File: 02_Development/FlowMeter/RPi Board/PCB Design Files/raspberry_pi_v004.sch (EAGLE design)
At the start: 116 parts, among them J5 POWER_JACK, P1 SPL006-007, P2 SPL006-007, P3 SPL006-007, P4 SPL006-007, P5 SPL006-007, Q1 4.3A/20V/54mΩ, Q2 500mA/300V, U6 TCA9548APWR, U7 TCA9548APWR

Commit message: added new 5V regulator
added new 5V regulator as existing regulator was out-of-stock at JLCPCB
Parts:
- removed C13: 33n, SparkFun-Capacitors:CAP-0805
- removed C23: 1uF, SparkFun-Capacitors:CAP-0805
- removed D3: 3A/40V/500mV, SparkFun-DiscreteSemi:DIODE-SCHOTTKY-B340A
- removed L1: INDUCTOR12.5, th_libraries:INDUCTOR12.5
- removed R1: 10K, SparkFun-Resistors:0.3OHM-0805-1/8W-1%
- removed R2: 3.3K, SparkFun-Resistors:0.3OHM-0805-1/8W-1%
- removed VREG1: XL4015, th_libraries:XL4015
- added C24: 100nF, SparkFun-Capacitors:CAP-0805
- added C25: 22uF, microbuilder:CAP_CERAMIC0805-NOOUTLINE
- added C27: 10uF, microbuilder:CAP_CERAMIC0805-NOOUTLINE
- added C28: 470nF, SparkFun-Capacitors:CAP-0805
- added C29: 4.7pF, SparkFun-Capacitors:CAP-0603
- added INDUCT: INDUCTOR_6.6_7.3, th_libraries:INDUCTOR_6.6_7.3
- added R49: 365K, SparkFun-Passives:RESISTOR0805-RES
- added R50: 49.9K, SparkFun-Passives:RESISTOR0805-RES
- added R51: 100K, SparkFun-Passives:RESISTOR0805-RES
- added R52: 10K, SparkFun-Resistors:0.3OHM-0805-1/8W-1%
- added TPS: TPS56528, th_libraries:TPS56528
- C19: value 1uF -> 10uF; device SparkFun-Capacitors:CAP-0805 -> microbuilder:CAP_CERAMIC0805-NOOUTLINE
- C20: value 1uF -> 100nF
- C22: value 220uF -> 22uF; device SparkFun-Capacitors:560UF-PANASONIC_G-25V-20% -> microbuilder:CAP_CERAMIC0805-NOOUTLINE
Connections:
- new net N$14: C24.1, TPS.VBST
- new net N$17: R51.1, TPS.PG
- new net N$27: R52.2, TPS.EN
- net 12V: now also C21.+, C27.1, R52.1, TPS.VIN; no longer C22.+, VREG1.IN
- net 5V: now also C22.1, C25.1, C29.1, INDUCT.2, R49.2; no longer C13.1, C21.+, C23.1, L1.1, R1.1
- net GND: now also C19.2, C22.2, C25.2, C27.2, C28.2, R50.2, TPS.GND, TPS.PWPD; no longer C22.-, C23.2, D3.A, R2.2, VREG1.GND
- net N$11: now also C29.2, R49.1, R50.1, TPS.VFB; no longer C13.2, R1.2, R2.1, VREG1.FB
- net N$6: now also C24.2, INDUCT.1, TPS.SW; no longer D3.C, L1.2, VREG1.SW
- net N$7: now also C28.1, R51.2, TPS.VREG; no longer C19.2, VREG1.VC
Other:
- note added: "3.3uH"
- note added: "Regulator - TPS56528DDAR https://datasheet.lcsc.com/szlcsc/1805310826_Texas-Instruments-TPS56528DDAR_C138716.pdf LCSC Part# C138716 Package SOIC - 150mill grounding pad Input Capacitor 330uF, 35V (only 25V required) LCSC Part# C134522 https://datasheet.lcsc.com/szlcsc/Lelon-VZH331M1VTR-1010K_C134522.pdf 10X10MM ROHS, panasonic G Inductor 3.3uH, 6.5amps MHCI06030-3R3M-R8A - 6.6x7.3mm LCSC Part# C2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"
- note added: "version 004 12/5/2020 - add new 5V regulator version 003 - removed piezo buzzer - used transistor/P-ch mosfet for triggering sensirion power - added 33nF capacitor on the 5V power regulator based on rev1.6 of the data sheet"
- note removed: "Regulator - XL4015E1 https://lcsc.com/product-detail/DC-DC-Converters_XL4015E1_C51661.html/?href=jlc-SMT LCSC Part# C51661 Package TO-263-5 Input capacitor Spec - 50V Selection 220uF, 50V LCSC Part# C134732 https://datasheet.lcsc.com/szlcsc/Lelon-VE-221M1HTR-1010_C134732.pdf 10X10MM ROHS, panasonic G Output Capacitor 330uF, 35V (only 25V required) LCSC Part# C134522 https://datasheet.lcsc.com/szl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"
- note removed: "version 003 - removed piezo buzzer - used transistor/P-ch mosfet for triggering sensirion power - added 33nF capacitor on the 5V power regulator based on rev1.6 of the data sheet"
- moved on the sheet: C19, C20, C21

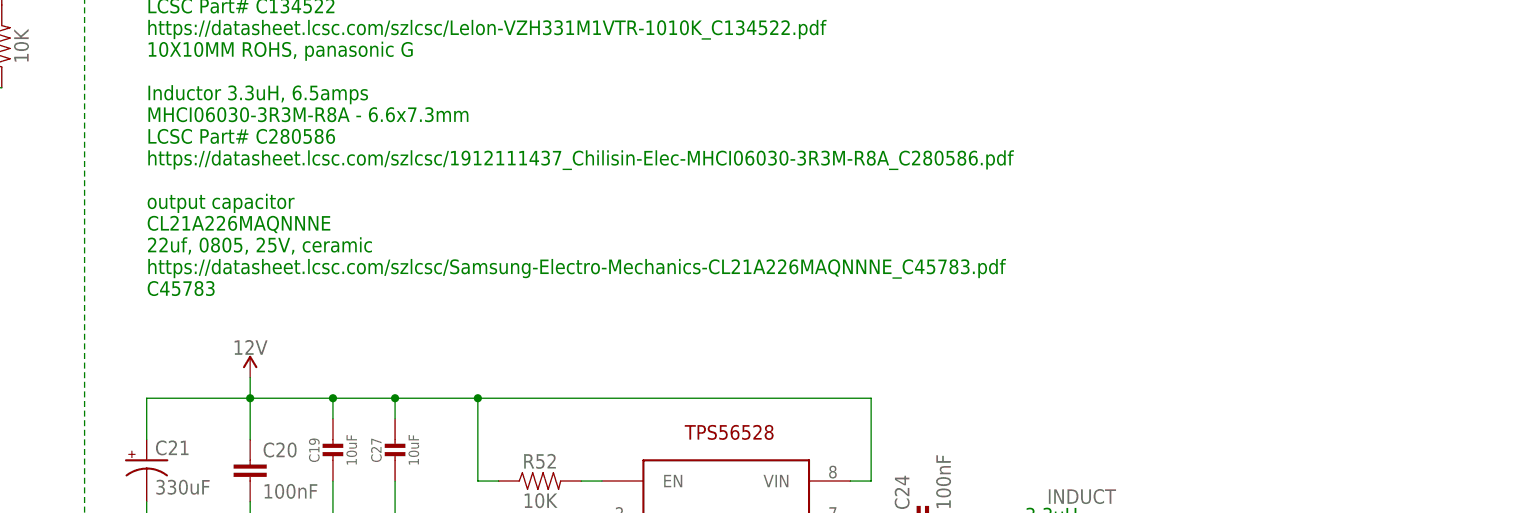
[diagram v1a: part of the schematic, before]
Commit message: updated capacitor
changed C22 and C25 to 1206 footprint and specified 2mohm low ESR cap
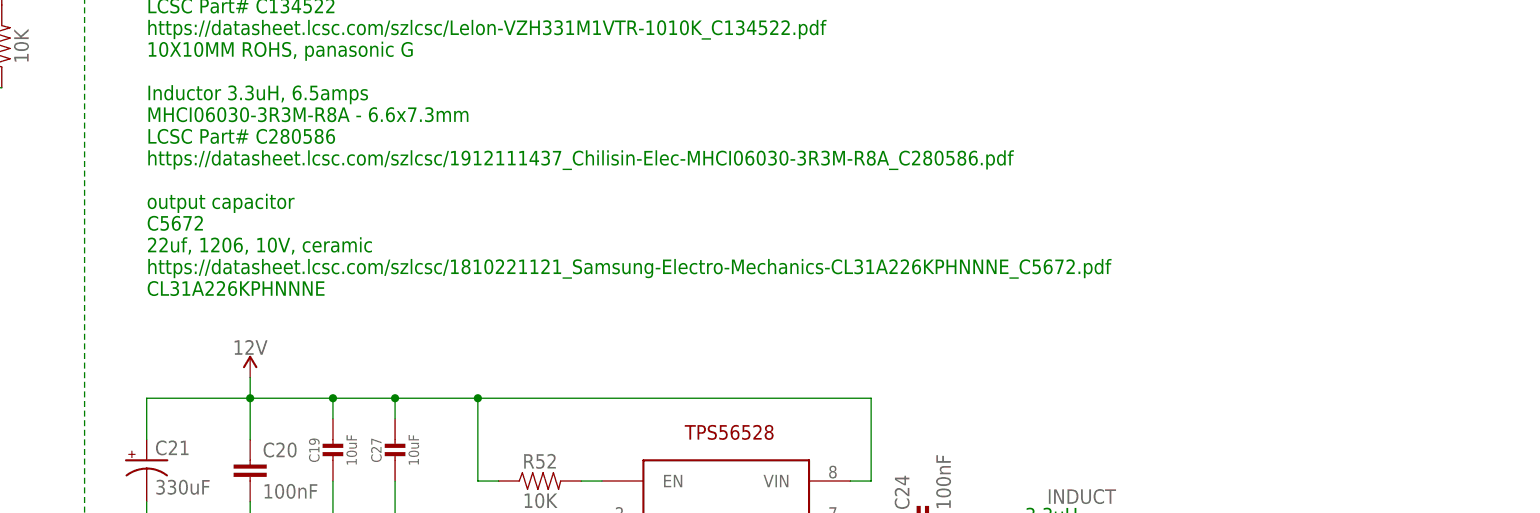
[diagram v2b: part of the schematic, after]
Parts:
- C22, C25: device microbuilder:CAP_CERAMIC0805-NOOUTLINE -> microbuilder:CAP_CERAMIC_1206
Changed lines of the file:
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@@
 <grid distance="0.1" unitdist="inch" unit="inch" style="lines" multiple="1" display="no" altdistance="0.01" altunitdist="inch" altunit="inch"/>
 <layers>
-<layer number="1" name="Top" color="4" fill="1" visible="no" active="no"/>
-<layer number="2" name="Route2" color="1" fill="3" visible="no" active="no"/>
-<layer number="3" name="Route3" color="4" fill="3" visible="no" active="no"/>
-<layer number="4" name="Route4" color="1" fill="4" visible="no" active="no"/>
-<layer number="5" name="Route5" color="4" fill="4" visible="no" active="no"/>
-<layer number="6" name="Route6" color="1" fill="8" visible="no" active="no"/>
-<layer number="7" name="Route7" color="4" fill="8" visible="no" active="no"/>
-<layer number="8" name="Route8" color="1" fill="2" visible="no" active="no"/>
-<layer number="9" name="Route9" color="4" fill="2" visible="no" active="no"/>
-<layer number="10" name="Route10" color="1" fill="7" visible="no" active="no"/>
-<layer number="11" name="Route11" color="4" fill="7" visible="no" active="no"/>
-<layer number="12" name="Route12" color="1" fill="5" visible="no" active="no"/>
-<layer number="13" name="Route13" color="4" fill="5" visible="no" active="no"/>
-<layer number="14" name="Route14" color="1" fill="6" visible="no" active="no"/>
-<layer number="15" name="Route15" color="4" fill="6" visible="no" active="no"/>
-<layer number="16" name="Bottom" color="1" fill="1" visible="no" active="no"/>
-<layer number="17" name="Pads" color="2" fill="1" visible="no" active="no"/>
-<layer number="18" name="Vias" color="2" fill="1" visible="no" active="no"/>
-<layer number="19" name="Unrouted" color="6" fill="1" visible="no" active="no"/>
-<layer number="20" name="Dimension" color="24" fill="1" visible="no" active="no"/>
-<layer number="21" name="tPlace" color="7" fill="1" visible="no" active="no"/>
-<layer number="22" name="bPlace" color="7" fill="1" visible="no" active="no"/>
-<layer number="23" name="tOrigins" color="15" fill="1" visible="no" active="no"/>
-<layer number="24" name="bOrigins" color="15" fill="1" visible="no" active="no"/>
-<layer number="25" name="tNames" color="7" fill="1" visible="no" active="no"/>
-<layer number="26" name="bNames" color="7" fill="1" visible="no" active="no"/>
-<layer number="27" name="tValues" color="7" fill="1" visible="no" active="no"/>
-<layer number="28" name="bValues" color="7" fill="1" visible="no" active="no"/>
+<layer number="1" name="Top" color="4" fill="1" visible="yes" active="no"/>
+<layer number="2" name="Route2" color="1" fill="3" visible="yes" active="no"/>
+<layer number="3" name="Route3" color="4" fill="3" visible="yes" active="no"/>
+<layer number="4" name="Route4" color="1" fill="4" visible="yes" active="no"/>
+<layer number="5" name="Route5" color="4" fill="4" visible="yes" active="no"/>
+<layer number="6" name="Route6" color="1" fill="8" visible="yes" active="no"/>
+<layer number="7" name="Route7" color="4" fill="8" visible="yes" active="no"/>
+<layer number="8" name="Route8" color="1" fill="2" visible="yes" active="no"/>
+<layer number="9" name="Route9" color="4" fill="2" visible="yes" active="no"/>
+<layer number="10" name="Route10" color="1" fill="7" visible="yes" active="no"/>
+<layer number="11" name="Route11" color="4" fill="7" visible="yes" active="no"/>
+<layer number="12" name="Route12" color="1" fill="5" visible="yes" active="no"/>
+<layer number="13" name="Route13" color="4" fill="5" visible="yes" active="no"/>
+<layer number="14" name="Route14" color="1" fill="6" visible="yes" active="no"/>
+<layer number="15" name="Route15" color="4" fill="6" visible="yes" active="no"/>
+<layer number="16" name="Bottom" color="1" fill="1" visible="yes" active="no"/>
+<layer number="17" name="Pads" color="2" fill="1" visible="yes" active="no"/>
+<layer number="18" name="Vias" color="2" fill="1" visible="yes" active="no"/>
+<layer number="19" name="Unrouted" color="6" fill="1" visible="yes" active="no"/>
+<layer number="20" name="Dimension" color="24" fill="1" visible="yes" active="no"/>
+<layer number="21" name="tPlace" color="7" fill="1" visible="yes" active="no"/>
+<layer number="22" name="bPlace" color="7" fill="1" visible="yes" active="no"/>
+<layer number="23" name="tOrigins" color="15" fill="1" visible="yes" active="no"/>
+<layer number="24" name="bOrigins" color="15" fill="1" visible="yes" active="no"/>
+<layer number="25" name="tNames" color="7" fill="1" visible="yes" active="no"/>
+<layer number="26" name="bNames" color="7" fill="1" visible="yes" active="no"/>
+<layer number="27" name="tValues" color="7" fill="1" visible="yes" active="no"/>
+<layer number="28" name="bValues" color="7" fill="1" visible="yes" active="no"/>
 <layer number="29" name="tStop" color="7" fill="3" visible="no" active="no"/>
 <layer number="30" name="bStop" color="7" fill="6" visible="no" active="no"/>
@@
 <layer number="35" name="tGlue" color="7" fill="4" visible="no" active="no"/>
 <layer number="36" name="bGlue" color="7" fill="5" visible="no" active="no"/>
-<layer number="37" name="tTest" color="7" fill="1" visible="no" active="no"/>
-<layer number="38" name="bTest" color="7" fill="1" visible="no" active="no"/>
+<layer number="37" name="tTest" color="7" fill="1" visible="yes" active="no"/>
+<layer number="38" name="bTest" color="7" fill="1" visible="yes" active="no"/>
 <layer number="39" name="tKeepout" color="4" fill="11" visible="no" active="no"/>
 <layer number="40" name="bKeepout" color="1" fill="11" visible="no" active="no"/>
@@
 <layer number="44" name="Drills" color="7" fill="1" visible="no" active="no"/>
 <layer number="45" name="Holes" color="7" fill="1" visible="no" active="no"/>
-<layer number="46" name="Milling" color="3" fill="1" visible="no" active="no"/>
-<layer number="47" name="Measures" color="7" fill="1" visible="no" active="no"/>
-<layer number="48" name="Document" color="7" fill="1" visible="no" active="no"/>
-<layer number="49" name="Reference" color="7" fill="1" visible="no" active="no"/>
-<layer number="50" name="dxf" color="7" fill="1" visible="no" active="no"/>
-<layer number="51" name="tDocu" color="7" fill="1" visible="no" active="no"/>
-<layer number="52" name="bDocu" color="7" fill="1" visible="no" active="no"/>
-<layer number="53" name="tGND_GNDA" color="7" fill="9" visible="no" active="no"/>
-<layer number="54" name="bGND_GNDA" color="1" fill="9" visible="no" active="no"/>
-<layer number="56" name="wert" color="7" fill="1" visible="no" active="no"/>
-<layer number="57" name="tCAD" color="7" fill="1" visible="no" active="no"/>
-<layer number="58" name="bCAD" color="11" fill="1" visible="no" active="no"/>
-<layer number="59" name="tCarbon" color="7" fill="1" visible="no" active="no"/>
-<layer number="60" name="bCarbon" color="7" fill="1" visible="no" active="no"/>
+<layer number="46" name="Milling" color="3" fill="1" visible="yes" active="no"/>
+<layer number="47" name="Measures" color="7" fill="1" visible="yes" active="no"/>
+<layer number="48" name="Document" color="7" fill="1" visible="yes" active="no"/>
+<layer number="49" name="Reference" color="7" fill="1" visible="yes" active="no"/>
+<layer number="50" name="dxf" color="7" fill="1" visible="yes" active="no"/>
+<layer number="51" name="tDocu" color="7" fill="1" visible="yes" active="no"/>
+<layer number="52" name="bDocu" color="7" fill="1" visible="yes" active="no"/>
+<layer number="53" name="tGND_GNDA" color="7" fill="9" visible="yes" active="no"/>
+<layer number="54" name="bGND_GNDA" color="1" fill="9" visible="yes" active="no"/>
+<layer number="56" name="wert" color="7" fill="1" visible="yes" active="no"/>
+<layer number="57" name="tCAD" color="7" fill="1" visible="yes" active="no"/>
+<layer number="58" name="bCAD" color="11" fill="1" visible="yes" active="no"/>
+<layer number="59" name="tCarbon" color="7" fill="1" visible="yes" active="no"/>
+<layer number="60" name="bCarbon" color="7" fill="1" visible="yes" active="no"/>
 <layer number="88" name="SimResults" color="9" fill="1" visible="yes" active="yes"/>
 <layer number="89" name="SimProbes" color="9" fill="1" visible="yes" active="yes"/>
@@
 <part name="R52" library="SparkFun-Resistors" deviceset="0.3OHM" device="-0805-1/8W-1%" value="10K"/>
 <part name="INDUCT" library="th_libraries" deviceset="INDUCTOR_6.6_7.3" device=""/>
-<part name="C22" library="microbuilder" deviceset="CAP_CERAMIC" device="0805-NOOUTLINE" value="22uF"/>
-<part name="C25" library="microbuilder" deviceset="CAP_CERAMIC" device="0805-NOOUTLINE" value="22uF"/>
+<part name="C22" library="microbuilder" deviceset="CAP_CERAMIC" device="_1206" value="22uF"/>
+<part name="C25" library="microbuilder" deviceset="CAP_CERAMIC" device="_1206" value="22uF"/>
 </parts>
 <sheets>
@@
 https://datasheet.lcsc.com/szlcsc/1912111437_Chilisin-Elec-MHCI06030-3R3M-R8A_C280586.pdf
 output capacitor
-CL21A226MAQNNNE
-22uf, 0805, 25V, ceramic
-https://datasheet.lcsc.com/szlcsc/Samsung-Electro-Mechanics-CL21A226MAQNNNE_C45783.pdf
-C45783
+C5672
+22uf, 1206, 10V, ceramic
+https://datasheet.lcsc.com/szlcsc/1810221121_Samsung-Electro-Mechanics-CL31A226KPHNNNE_C5672.pdf
+CL31A226KPHNNNE
 </text>
 <text x="297.18" y="167.132" size="1.778" layer="91">i2C Multiplexier

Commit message: Next revision of PCB (#152)
* Next revision of PCB

Changed I2C pullup resistors to 3Kohm

General tidy up and fix of issues on the PCB. Tweaked some polygons to eliminate sharp corners, made some traces larger.

* Changes made as per PR152

Changes made as requested, I also updated the pdf of the schematic and the dru file.

One thing I have noticed is that generating the BOM automatically comes up with the incorrect resistor value of 0.3 Ohms. I suspect this is to do with the library that is being used.

* Create READ ME BEFORE CONTINUING.md

Added a cautionary text file to explain the issue with the automatically generated BOM and the incorrect resistor values being utilised.
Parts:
- R10, R13, R14, R15, R16, R17, R18, R29, R30, R31, R32, R33, R34, R35, R36, R7, R8, R9: value 10K -> 3K
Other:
- note added: "version 005 14/12/2020 editor Darragh Broadbent - changed pull up resistor value between I2C multiplexer and slave devices to 3K from 10K - resolved clearance issues version 004 12/5/2020 - add new 5V regulator version 003 - removed piezo buzzer - used transistor/P-ch mosfet for triggering sensirion power - added 33nF capacitor on the 5V power regulator based on rev1.6 of the data sheet"
- note removed: "version 004 12/5/2020 - add new 5V regulator version 003 - removed piezo buzzer - used transistor/P-ch mosfet for triggering sensirion power - added 33nF capacitor on the 5V power regulator based on rev1.6 of the data sheet"
